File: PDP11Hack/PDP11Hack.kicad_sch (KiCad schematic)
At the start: 0 parts

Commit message: Finished schematic
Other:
- added sheet UART (UART.kicad_sch)

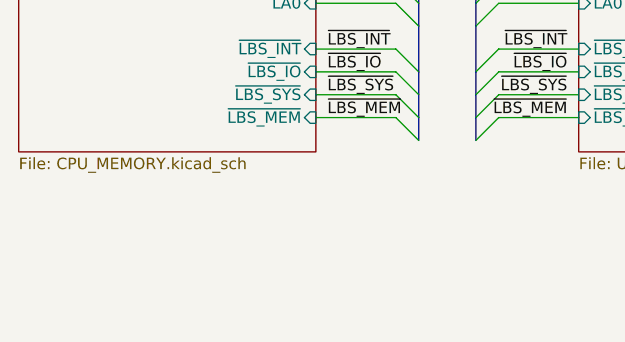
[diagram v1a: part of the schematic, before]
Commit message: Assigned footprints.
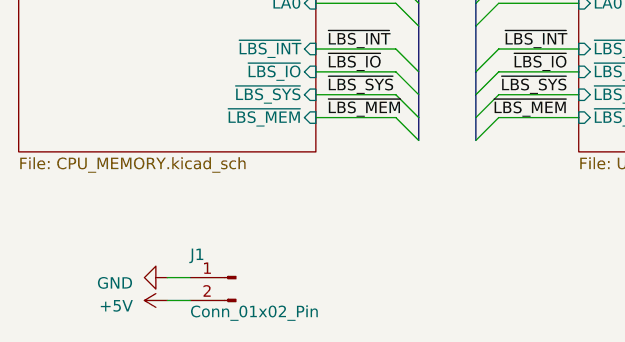
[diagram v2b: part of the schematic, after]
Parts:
- added J1: Conn_01x02_Pin, Connector_PinHeader_1.27mm:PinHeader_1x02_P1.27mm_Vertical, symbol Connector:Conn_01x02_Pin
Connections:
- new net +5V: J1.2 (Pin_2)
- new net GND: J1.1 (Pin_1)
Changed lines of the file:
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@@
+    (stroke (width 0) (type default))
+  )
+  (wire (pts (xy 44.45 160.02) (xy 46.99 160.02))
     (stroke (width 0) (type default))
   )
@@
     (stroke (width 0) (type default))
   )
+  (wire (pts (xy 44.45 157.48) (xy 46.99 157.48))
+    (stroke (width 0) (type default))
+  )
   (bus (pts (xy 78.74 68.58) (xy 78.74 71.12))
     (stroke (width 0) (type default))
@@
     (effects (font (size 1.27 1.27)) (justify left bottom))
   )
+  (symbol (lib_id "power:GND") (at 44.45 157.48 270) (unit 1)
+    (in_bom yes) (on_board yes) (dnp no) (fields_autoplaced)
+    (property "Reference" "#PWR040" (at 38.1 157.48 0)
+      (effects (font (size 1.27 1.27)) hide)
+    )
+    (property "Value" "GND" (at 40.64 158.115 90)
+      (effects (font (size 1.27 1.27)) (justify right))
+    )
+    (property "Footprint" "" (at 44.45 157.48 0)
+      (effects (font (size 1.27 1.27)) hide)
+    )
+    (property "Datasheet" "" (at 44.45 157.48 0)
+      (effects (font (size 1.27 1.27)) hide)
+    )
+    (pin "1")
+    (instances
+      (project "PDP11Hack"
+        (path "/8ff9937c-7c0e-4cdc-97b3-aa12bc435179"
+          (reference "#PWR040") (unit 1)
+        )
+      )
+    )
+  )
+  (symbol (lib_id "power:+5V") (at 44.45 160.02 90) (unit 1)
+    (in_bom yes) (on_board yes) (dnp no) (fields_autoplaced)
+    (property "Reference" "#PWR041" (at 48.26 160.02 0)
+      (effects (font (size 1.27 1.27)) hide)
+    )
+    (property "Value" "+5V" (at 40.64 160.655 90)
+      (effects (font (size 1.27 1.27)) (justify left))
+    )
+    (property "Footprint" "" (at 44.45 160.02 0)
+      (effects (font (size 1.27 1.27)) hide)
+    )
+    (property "Datasheet" "" (at 44.45 160.02 0)
+      (effects (font (size 1.27 1.27)) hide)
+    )
+    (pin "1")
+    (instances
+      (project "PDP11Hack"
+        (path "/8ff9937c-7c0e-4cdc-97b3-aa12bc435179"
+          (reference "#PWR041") (unit 1)
+        )
+      )
+    )
+  )
+  (symbol (lib_id "Connector:Conn_01x02_Pin") (at 52.07 157.48 0) (mirror y) (unit 1)
+    (in_bom yes) (on_board yes) (dnp no)
+    (property "Reference" "J1" (at 46.99 154.94 0)
+      (effects (font (size 1.27 1.27)) (justify right))
+    )
+    (property "Value" "Conn_01x02_Pin" (at 46.99 161.29 0)
+      (effects (font (size 1.27 1.27)) (justify right))
+    )
+    (property "Footprint" "Connector_PinHeader_1.27mm:PinHeader_1x02_P1.27mm_Vertical" (at 52.07 157.48 0)
+      (effects (font (size 1.27 1.27)) hide)
+    )
+    (property "Datasheet" "~" (at 52.07 157.48 0)
+      (effects (font (size 1.27 1.27)) hide)
+    )
+    (pin "1")
+    (pin "2")
+    (instances
+      (project "PDP11Hack"
+        (path "/8ff9937c-7c0e-4cdc-97b3-aa12bc435179/803520a2-1026-4643-ad50-3a6c51ceb386"
+          (reference "J1") (unit 1)
+        )
+        (path "/8ff9937c-7c0e-4cdc-97b3-aa12bc435179"
+          (reference "J3") (unit 1)
+        )
+      )
+    )
+  )
   (sheet (at 90.17 31.75) (size 33.02 111.76) (fields_autoplaced)
